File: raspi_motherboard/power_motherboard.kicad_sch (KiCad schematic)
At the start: 19 parts, among them J1 GPIO, J2 Conn_02x04_Top_Bottom

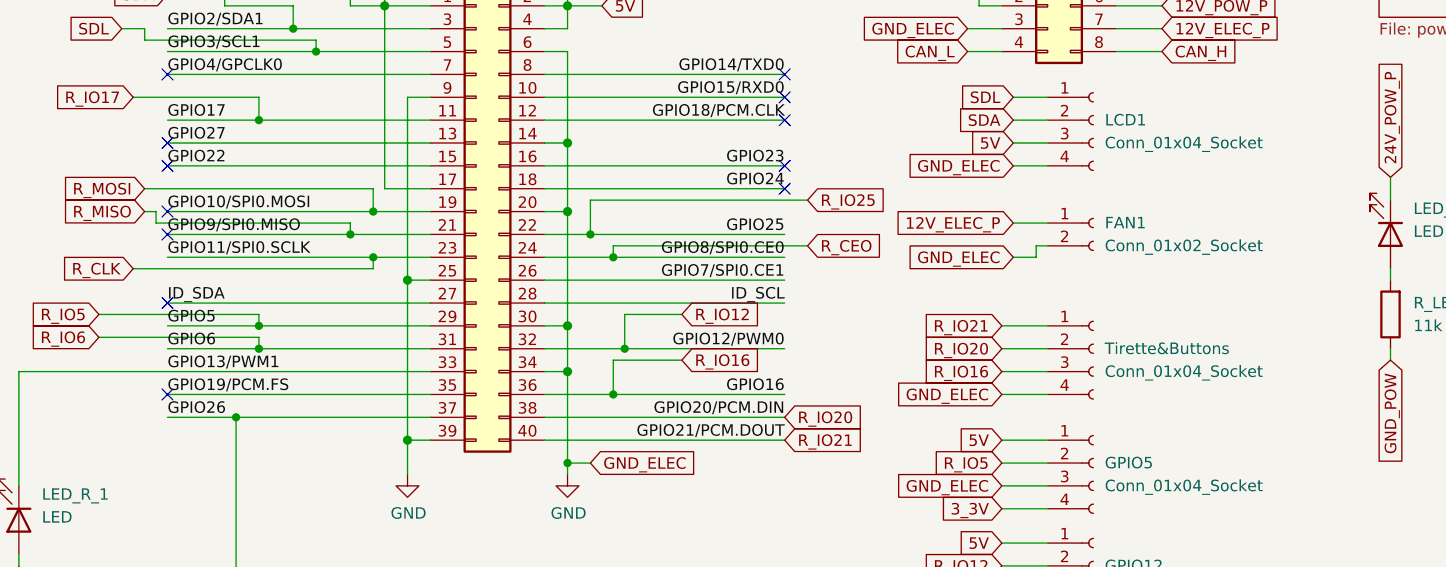
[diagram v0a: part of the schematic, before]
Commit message: fix ERC/DRC (including short-circuits) + add flood fills
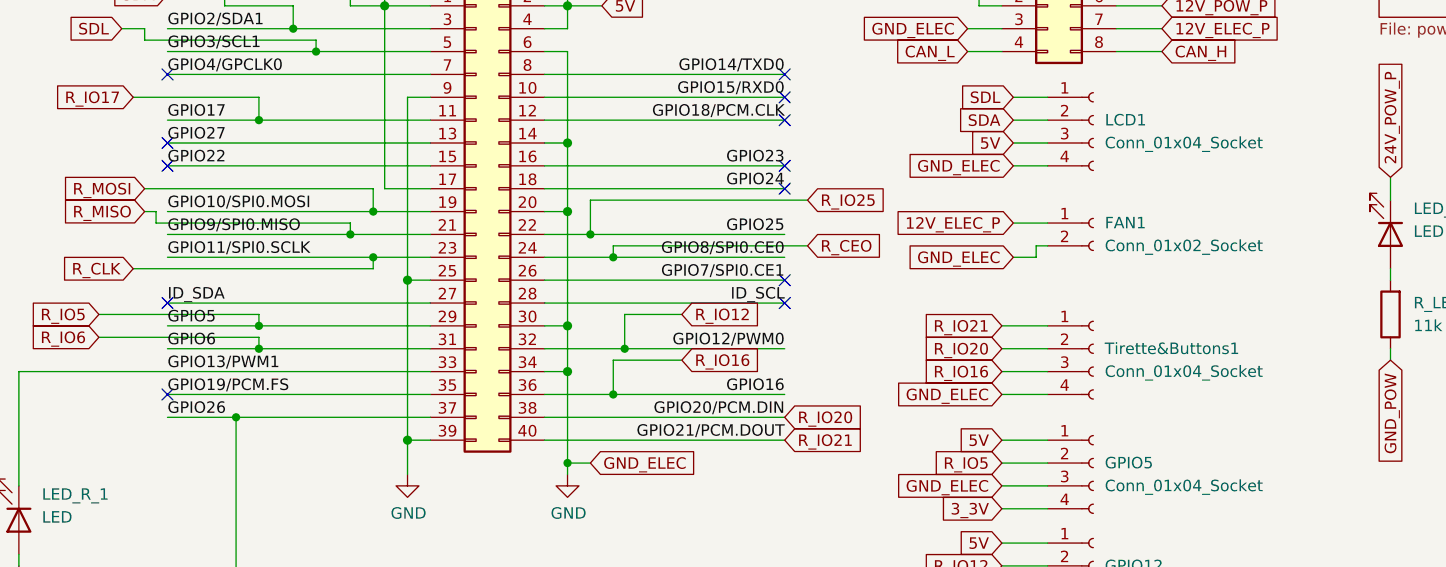
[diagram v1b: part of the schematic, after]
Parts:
- renumbered Tirette&Buttons to Tirette&Buttons1
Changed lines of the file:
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@@
 	)
 	(no_connect
+		(at 100.33 58.42)
+	)
+	(no_connect
 		(at 31.75 35.56)
 	)
@@
 	)
 	(no_connect
-		(at 31.75 50.8)
-	)
-	(no_connect
-		(at 31.75 53.34)
+		(at 100.33 60.96)
 	)
 	(no_connect
@@
 	(label "ID_SDA"
 		(at 31.75 60.96 0)
-		(fields_autoplaced yes)
 		(effects
 			(font
@@
 	(label "GPIO6"
 		(at 31.75 66.04 0)
-		(fields_autoplaced yes)
 		(effects
 			(font
@@
 	(label "ID_SCL"
 		(at 100.33 60.96 180)
-		(fields_autoplaced yes)
 		(effects
 			(font
@@
 	(label "GPIO5"
 		(at 31.75 63.5 0)
-		(fields_autoplaced yes)
 		(effects
 			(font
@@
 	(label "GPIO21{slash}PCM.DOUT"
 		(at 100.33 76.2 180)
-		(fields_autoplaced yes)
 		(effects
 			(font
@@
 	(label "GPIO19{slash}PCM.FS"
 		(at 31.75 71.12 0)
-		(fields_autoplaced yes)
 		(effects
 			(font
@@
 	(label "GPIO10{slash}SPI0.MOSI"
 		(at 31.75 50.8 0)
-		(fields_autoplaced yes)
 		(effects
 			(font
@@
 	(label "GPIO9{slash}SPI0.MISO"
 		(at 31.75 53.34 0)
-		(fields_autoplaced yes)
 		(effects
 			(font
@@
 	(label "GPIO23"
 		(at 100.33 45.72 180)
-		(fields_autoplaced yes)
 		(effects
 			(font
@@
 	(label "GPIO4{slash}GPCLK0"
 		(at 31.75 35.56 0)
-		(fields_autoplaced yes)
 		(effects
 			(font
@@
 	(label "GPIO27"
 		(at 31.75 43.18 0)
-		(fields_autoplaced yes)
 		(effects
 			(font
@@
 	(label "GPIO26"
 		(at 31.75 73.66 0)
-		(fields_autoplaced yes)
 		(effects
 			(font
@@
 	(label "GPIO14{slash}TXD0"
 		(at 100.33 35.56 180)
-		(fields_autoplaced yes)
 		(effects
 			(font
@@
 	(label "GPIO8{slash}SPI0.CE0"
 		(at 100.33 55.88 180)
-		(fields_autoplaced yes)
 		(effects
 			(font
@@
 	(label "GPIO15{slash}RXD0"
 		(at 100.33 38.1 180)
-		(fields_autoplaced yes)
 		(effects
 			(font
@@
 	(label "GPIO16"
 		(at 100.33 71.12 180)
-		(fields_autoplaced yes)
 		(effects
 			(font
@@
 	(label "GPIO22"
 		(at 31.75 45.72 0)
-		(fields_autoplaced yes)
 		(effects
 			(font
@@
 	(label "GPIO2{slash}SDA1"
 		(at 31.75 30.48 0)
-		(fields_autoplaced yes)
 		(effects
 			(font
@@
 	(label "GPIO17"
 		(at 31.75 40.64 0)
-		(fields_autoplaced yes)
 		(effects
 			(font
@@
 	(label "GPIO25"
 		(at 100.33 53.34 180)
-		(fields_autoplaced yes)
 		(effects
 			(font
@@
 	(label "GPIO3{slash}SCL1"
 		(at 31.75 33.02 0)
-		(fields_autoplaced yes)
 		(effects
 			(font
@@
 	(label "GPIO18{slash}PCM.CLK"
 		(at 100.33 40.64 180)
-		(fields_autoplaced yes)
 		(effects
 			(font
@@
 	(label "GPIO12{slash}PWM0"
 		(at 100.33 66.04 180)
-		(fields_autoplaced yes)
 		(effects
 			(font
@@
 	(label "GPIO13{slash}PWM1"
 		(at 31.75 68.58 0)
-		(fields_autoplaced yes)
 		(effects
 			(font
@@
 	(label "GPIO20{slash}PCM.DIN"
 		(at 100.33 73.66 180)
-		(fields_autoplaced yes)
 		(effects
 			(font
@@
 	(label "GPIO24"
 		(at 100.33 48.26 180)
-		(fields_autoplaced yes)
 		(effects
 			(font
@@
 	(label "GPIO7{slash}SPI0.CE1"
 		(at 100.33 58.42 180)
-		(fields_autoplaced yes)
 		(effects
 			(font
@@
 	(label "GPIO11{slash}SPI0.SCLK"
 		(at 31.75 55.88 0)
-		(fields_autoplaced yes)
 		(effects
 			(font
@@
 		(dnp no)
 		(fields_autoplaced yes)
-		(property "Reference" "Tirette&Buttons"
+		(property "Reference" "Tirette&Buttons1"
 			(at 135.89 66.0399 0)
 			(effects
@@
 			(project "power_motherboard"
 				(path "/e63e39d7-6ac0-4ffd-8aa3-1841a4541b55"
-					(reference "Tirette&Buttons")
+					(reference "Tirette&Buttons1")
 					(unit 1)
 				)

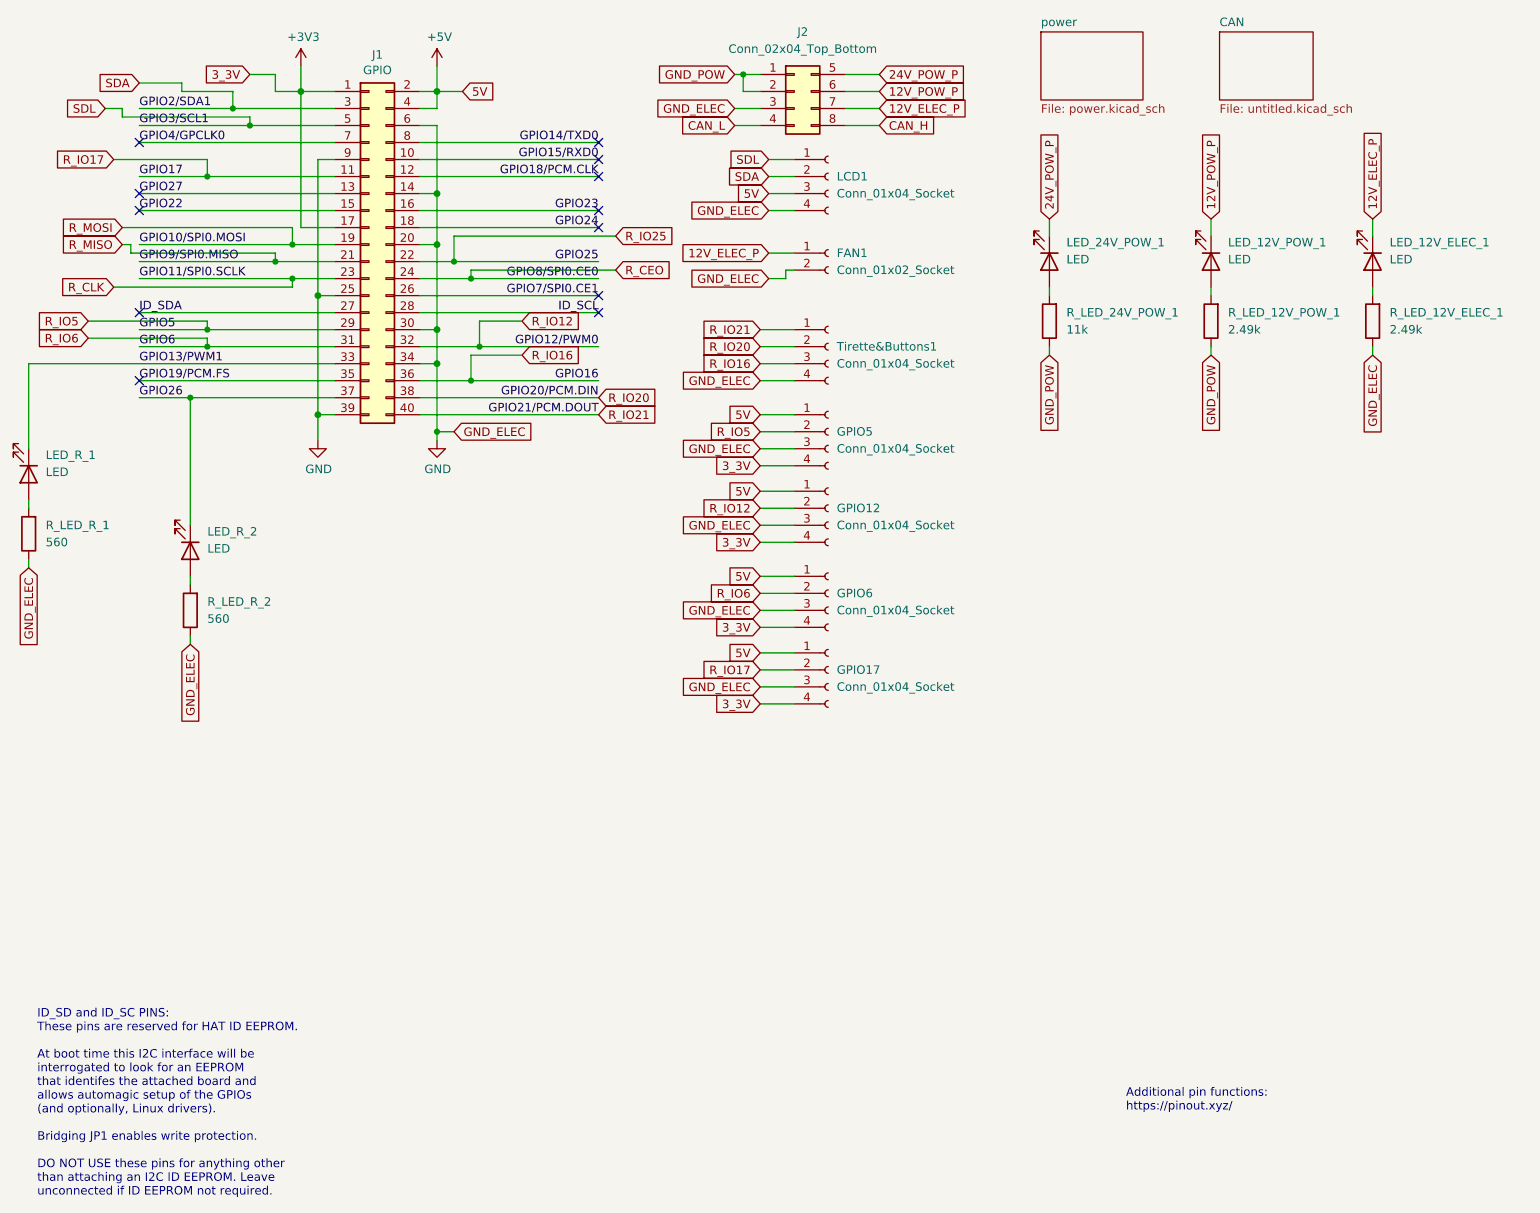
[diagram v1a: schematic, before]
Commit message: [WiP] start putting refs in silkscreen
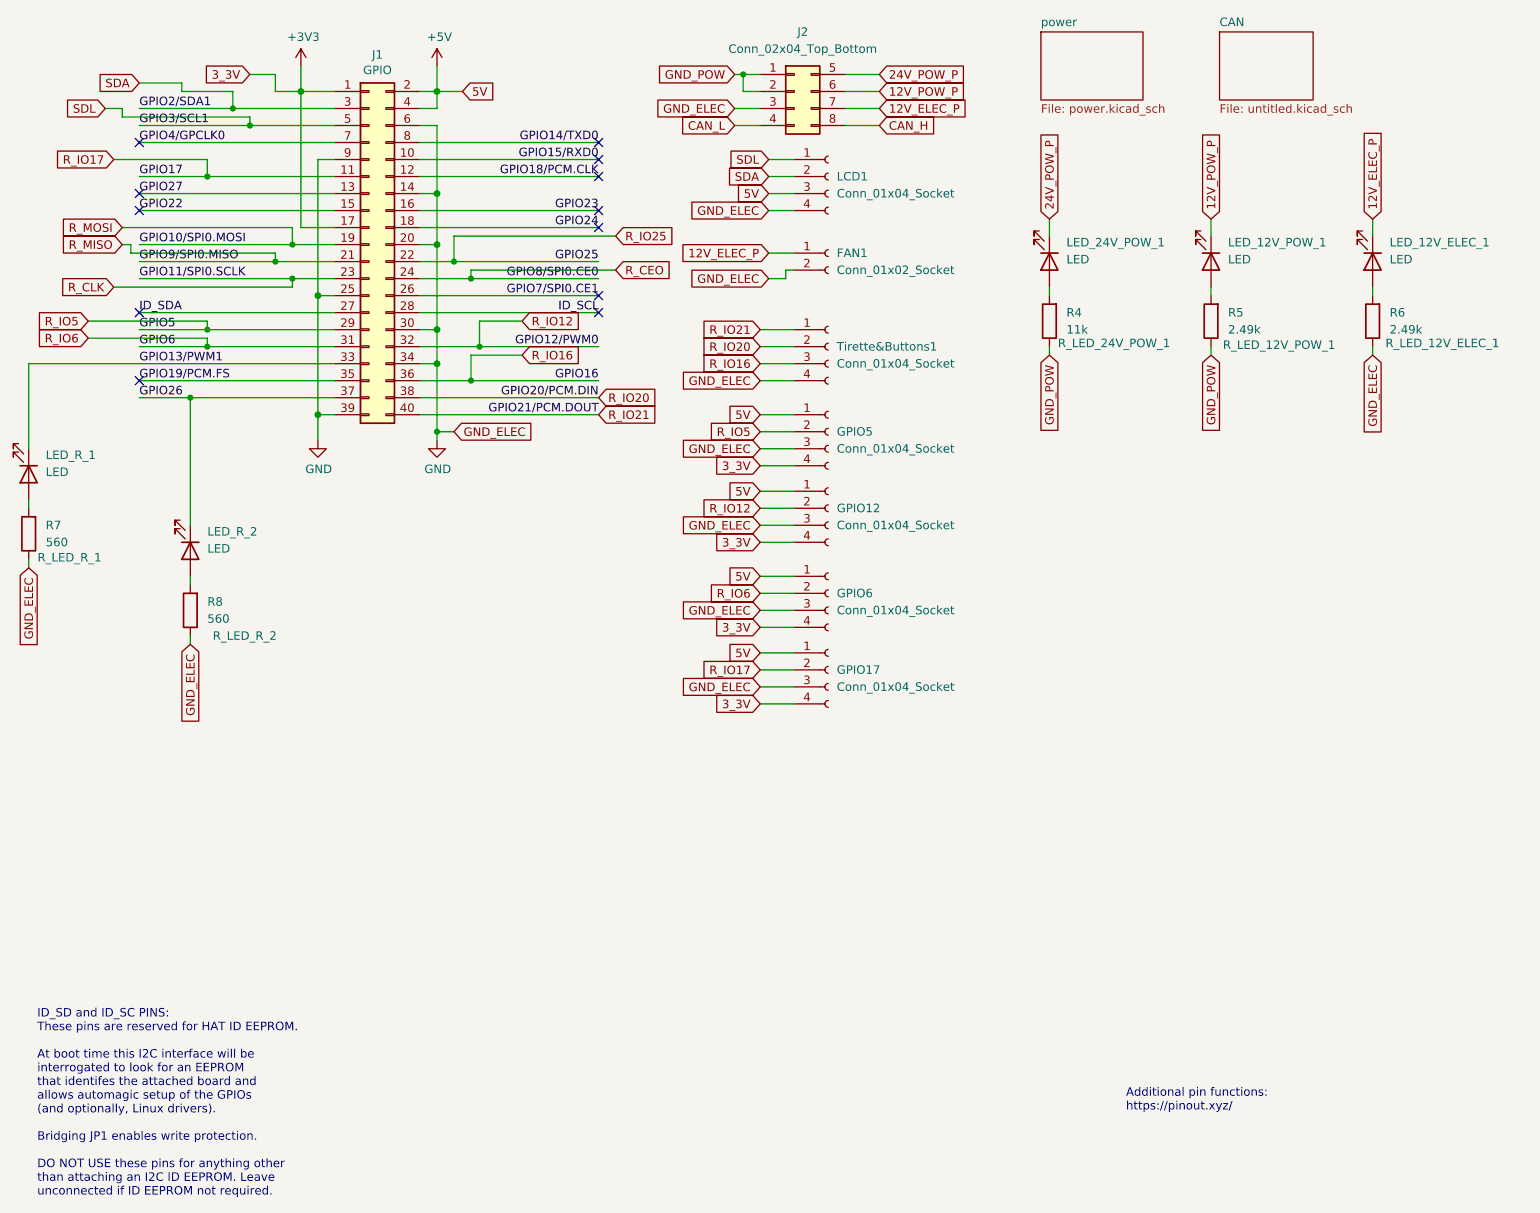
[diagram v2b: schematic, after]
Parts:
- renumbered R_LED_24V_POW_1 to R4, R_LED_12V_POW_1 to R5, R_LED_12V_ELEC_1 to R6, R_LED_R_1 to R7, R_LED_R_2 to R8
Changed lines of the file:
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@@
 	(label "ID_SDA"
 		(at 31.75 60.96 0)
+		(fields_autoplaced yes)
 		(effects
 			(font
@@
 	(label "GPIO6"
 		(at 31.75 66.04 0)
+		(fields_autoplaced yes)
 		(effects
 			(font
@@
 	(label "ID_SCL"
 		(at 100.33 60.96 180)
+		(fields_autoplaced yes)
 		(effects
 			(font
@@
 	(label "GPIO5"
 		(at 31.75 63.5 0)
+		(fields_autoplaced yes)
 		(effects
 			(font
@@
 	(label "GPIO21{slash}PCM.DOUT"
 		(at 100.33 76.2 180)
+		(fields_autoplaced yes)
 		(effects
 			(font
@@
 	(label "GPIO19{slash}PCM.FS"
 		(at 31.75 71.12 0)
+		(fields_autoplaced yes)
 		(effects
 			(font
@@
 	(label "GPIO10{slash}SPI0.MOSI"
 		(at 31.75 50.8 0)
+		(fields_autoplaced yes)
 		(effects
 			(font
@@
 	(label "GPIO9{slash}SPI0.MISO"
 		(at 31.75 53.34 0)
+		(fields_autoplaced yes)
 		(effects
 			(font
@@
 	(label "GPIO23"
 		(at 100.33 45.72 180)
+		(fields_autoplaced yes)
 		(effects
 			(font
@@
 	(label "GPIO4{slash}GPCLK0"
 		(at 31.75 35.56 0)
+		(fields_autoplaced yes)
 		(effects
 			(font
@@
 	(label "GPIO27"
 		(at 31.75 43.18 0)
+		(fields_autoplaced yes)
 		(effects
 			(font
@@
 	(label "GPIO26"
 		(at 31.75 73.66 0)
+		(fields_autoplaced yes)
 		(effects
 			(font
@@
 	(label "GPIO14{slash}TXD0"
 		(at 100.33 35.56 180)
+		(fields_autoplaced yes)
 		(effects
 			(font
@@
 	(label "GPIO8{slash}SPI0.CE0"
 		(at 100.33 55.88 180)
+		(fields_autoplaced yes)
 		(effects
 			(font
@@
 	(label "GPIO15{slash}RXD0"
 		(at 100.33 38.1 180)
+		(fields_autoplaced yes)
 		(effects
 			(font
@@
 	(label "GPIO16"
 		(at 100.33 71.12 180)
+		(fields_autoplaced yes)
 		(effects
 			(font
@@
 	(label "GPIO22"
 		(at 31.75 45.72 0)
+		(fields_autoplaced yes)
 		(effects
 			(font
@@
 	(label "GPIO2{slash}SDA1"
 		(at 31.75 30.48 0)
+		(fields_autoplaced yes)
 		(effects
 			(font
@@
 	(label "GPIO17"
 		(at 31.75 40.64 0)
+		(fields_autoplaced yes)
 		(effects
 			(font
@@
 	(label "GPIO25"
 		(at 100.33 53.34 180)
+		(fields_autoplaced yes)
 		(effects
 			(font
@@
 	(label "GPIO3{slash}SCL1"
 		(at 31.75 33.02 0)
+		(fields_autoplaced yes)
 		(effects
 			(font
@@
 	(label "GPIO18{slash}PCM.CLK"
 		(at 100.33 40.64 180)
+		(fields_autoplaced yes)
 		(effects
 			(font
@@
 	(label "GPIO12{slash}PWM0"
 		(at 100.33 66.04 180)
+		(fields_autoplaced yes)
 		(effects
 			(font
@@
 	(label "GPIO13{slash}PWM1"
 		(at 31.75 68.58 0)
+		(fields_autoplaced yes)
 		(effects
 			(font
@@
 	(label "GPIO20{slash}PCM.DIN"
 		(at 100.33 73.66 180)
+		(fields_autoplaced yes)
 		(effects
 			(font
@@
 	(label "GPIO24"
 		(at 100.33 48.26 180)
+		(fields_autoplaced yes)
 		(effects
 			(font
@@
 	(label "GPIO7{slash}SPI0.CE1"
 		(at 100.33 58.42 180)
+		(fields_autoplaced yes)
 		(effects
 			(font
@@
 	(label "GPIO11{slash}SPI0.SCLK"
 		(at 31.75 55.88 0)
+		(fields_autoplaced yes)
 		(effects
 			(font
@@
 		(on_board yes)
 		(dnp no)
-		(fields_autoplaced yes)
-		(property "Reference" "R_LED_24V_POW_1"
+		(property "Reference" "R4"
 			(at 170.18 60.96 0)
 			(effects
@@
 			)
 		)
-		(property "Description" ""
-			(at 167.64 62.23 0)
-			(effects
-				(font
-					(size 1.27 1.27)
-				)
-				(hide yes)
+		(property "Description" "R_LED_24V_POW_1"
+			(at 168.91 65.532 0)
+			(effects
+				(font
+					(size 1.27 1.27)
+				)
+				(justify right)
 			)
 		)
@@
 			(project "power_motherboard"
 				(path "/e63e39d7-6ac0-4ffd-8aa3-1841a4541b55"
-					(reference "R_LED_24V_POW_1")
+					(reference "R4")
 					(unit 1)
 				)
@@
 		(on_board yes)
 		(dnp no)
-		(fields_autoplaced yes)
-		(property "Reference" "R_LED_12V_POW_1"
+		(property "Reference" "R5"
 			(at 194.31 60.96 0)
 			(effects
@@
 			)
 		)
-		(property "Description" ""
-			(at 191.77 62.23 0)
-			(effects
-				(font
-					(size 1.27 1.27)
-				)
-				(hide yes)
+		(property "Description" "R_LED_12V_POW_1"
+			(at 201.93 65.786 0)
+			(effects
+				(font
+					(size 1.27 1.27)
+				)
 			)
 		)
@@
 			(project "power_motherboard"
 				(path "/e63e39d7-6ac0-4ffd-8aa3-1841a4541b55"
-					(reference "R_LED_12V_POW_1")
+					(reference "R5")
 					(unit 1)
 				)
@@
 		(on_board yes)
 		(dnp no)
-		(fields_autoplaced yes)
-		(property "Reference" "R_LED_12V_ELEC_1"
+		(property "Reference" "R6"
 			(at 218.44 60.96 0)
 			(effects
@@
 			)
 		)
-		(property "Description" ""
-			(at 215.9 62.23 0)
-			(effects
-				(font
-					(size 1.27 1.27)
-				)
-				(hide yes)
+		(property "Description" "R_LED_12V_ELEC_1"
+			(at 226.314 65.532 0)
+			(effects
+				(font
+					(size 1.27 1.27)
+				)
 			)
 		)
@@
 			(project "power_motherboard"
 				(path "/e63e39d7-6ac0-4ffd-8aa3-1841a4541b55"
-					(reference "R_LED_12V_ELEC_1")
+					(reference "R6")
 					(unit 1)
 				)
@@
 		(on_board yes)
 		(dnp no)
-		(fields_autoplaced yes)
-		(property "Reference" "R_LED_R_1"
+		(property "Reference" "R7"
 			(at 17.78 92.71 0)
 			(effects
@@
 			)
 		)
-		(property "Description" ""
-			(at 15.24 93.98 0)
-			(effects
-				(font
-					(size 1.27 1.27)
-				)
-				(hide yes)
+		(property "Description" "R_LED_R_1"
+			(at 21.336 97.536 0)
+			(effects
+				(font
+					(size 1.27 1.27)
+				)
 			)
 		)
@@
 			(project "power_motherboard"
 				(path "/e63e39d7-6ac0-4ffd-8aa3-1841a4541b55"
-					(reference "R_LED_R_1")
+					(reference "R7")
 					(unit 1)
 				)
@@
 		(on_board yes)
 		(dnp no)
-		(fields_autoplaced yes)
-		(property "Reference" "R_LED_R_2"
+		(property "Reference" "R8"
 			(at 41.91 104.14 0)
 			(effects
@@
 			)
 		)
-		(property "Description" ""
-			(at 39.37 105.41 0)
-			(effects
-				(font
-					(size 1.27 1.27)
-				)
-				(hide yes)
+		(property "Description" "R_LED_R_2"
+			(at 47.498 109.22 0)
+			(effects
+				(font
+					(size 1.27 1.27)
+				)
 			)
 		)
@@
 			(project "power_motherboard"
 				(path "/e63e39d7-6ac0-4ffd-8aa3-1841a4541b55"
-					(reference "R_LED_R_2")
+					(reference "R8")
 					(unit 1)
 				)
